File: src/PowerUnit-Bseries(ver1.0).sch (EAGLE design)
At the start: 46 parts

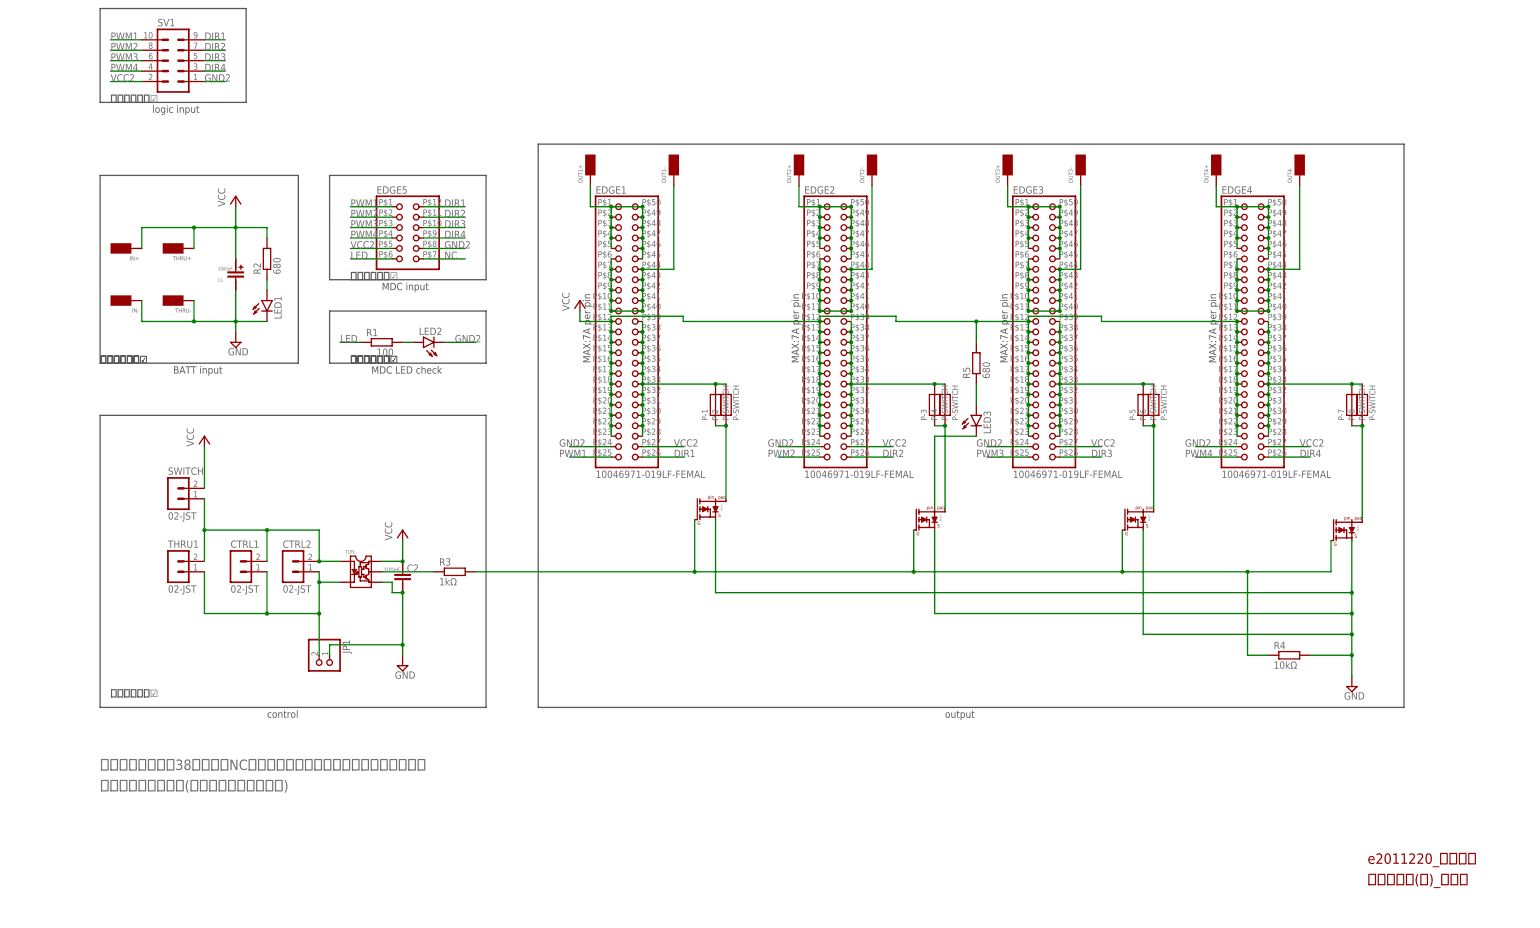
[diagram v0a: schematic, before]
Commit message: 再設計 Edgeコネクタを40Pにした
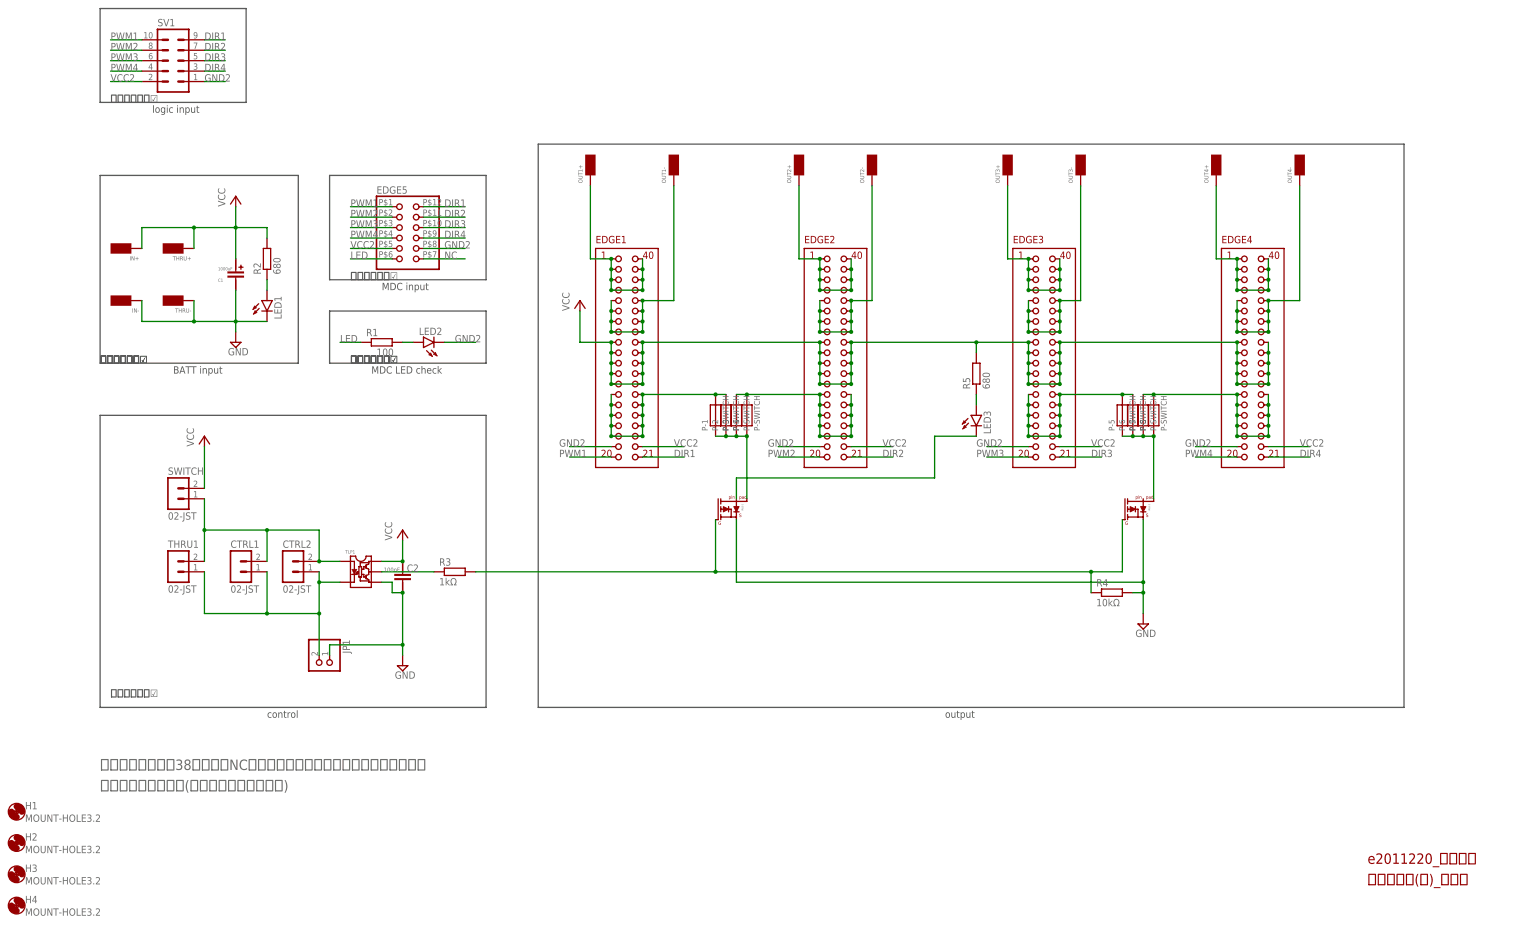
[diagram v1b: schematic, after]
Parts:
- removed IRLB-3, IRLB-4: IRLB3813_2, OKUDA_libraries:IRLB3813_2
- added H1, H2, H3, H4: MOUNT-HOLE3.2, holes:MOUNT-HOLE3.2
- EDGE1, EDGE2, EDGE3, EDGE4: value 10046971-019LF-FEMAL -> EDGE20X2; device 10046971-019LF-FEMAL:10046971-019LF-FEMAL -> Edge20x2:EDGE20X2
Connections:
- removed net N$10: EDGE4.P1, EDGE4.P2, EDGE4.P3, EDGE4.P4, EDGE4.P45, EDGE4.P46, EDGE4.P47, EDGE4.P48, EDGE4.P49, EDGE4.P5, EDGE4.P50, OUT4+.P$1
- removed net N$12: IRLB-4.PD, P-7.P$2, P-8.P$2
- removed net N$13: EDGE4.P10, EDGE4.P11, EDGE4.P40, EDGE4.P41, EDGE4.P42, EDGE4.P43, EDGE4.P44, EDGE4.P6, EDGE4.P7, EDGE4.P8, EDGE4.P9, OUT4-.P$1
- removed net N$14: EDGE3.P28, EDGE3.P29, EDGE3.P30, EDGE3.P31, EDGE3.P32, EDGE3.P33, EDGE3.P34, EDGE3.P35, EDGE3.P36, EDGE3.P37, EDGE3.P38, EDGE3.P39, P-5.P$1, P-6.P$1
- removed net N$15: IRLB-3.PD, P-5.P$2, P-6.P$2
- removed net N$25: EDGE1.P28, EDGE1.P29, EDGE1.P30, EDGE1.P31, EDGE1.P32, EDGE1.P33, EDGE1.P34, EDGE1.P35, EDGE1.P36, EDGE1.P37, EDGE1.P38, EDGE1.P39, P-1.P$1, P-2.P$1
- removed net N$26: EDGE2.P28, EDGE2.P29, EDGE2.P30, EDGE2.P31, EDGE2.P32, EDGE2.P33, EDGE2.P34, EDGE2.P35, EDGE2.P36, EDGE2.P37, EDGE2.P38, EDGE2.P39, P-3.P$1, P-4.P$1
- new net N$23: IRLB-1.PD, P-1.P$2, P-2.P$2, P-3.P$2, P-4.P$2
- new net N$27: IRLB-2.PD, P-5.P$2, P-6.P$2, P-7.P$2, P-8.P$2
- new net N$28: EDGE1.P$1, EDGE1.P$2, EDGE1.P$3, EDGE1.P$37, EDGE1.P$38, EDGE1.P$39, EDGE1.P$4, EDGE1.P$40, OUT1+.P$1
- new net N$34: EDGE2.P$14, EDGE2.P$15, EDGE2.P$16, EDGE2.P$17, EDGE2.P$18, EDGE2.P$23, EDGE2.P$24, EDGE2.P$25, EDGE2.P$26, EDGE2.P$27, P-3.P$1, P-4.P$1
- new net N$35: EDGE3.P$1, EDGE3.P$2, EDGE3.P$3, EDGE3.P$37, EDGE3.P$38, EDGE3.P$39, EDGE3.P$4, EDGE3.P$40, OUT3+.P$1
- net DIR1: now also EDGE1.P$21; no longer EDGE1.P26
- net DIR2: now also EDGE2.P$21; no longer EDGE2.P26
- net DIR3: now also EDGE3.P$21; no longer EDGE3.P26
- net DIR4: now also EDGE4.P$21; no longer EDGE4.P26
- net GND: no longer IRLB-3.S, IRLB-4.S
- net GND2: now also EDGE1.P$19, EDGE2.P$19, EDGE3.P$19, EDGE4.P$19; no longer EDGE1.P24, EDGE2.P24, EDGE3.P24, EDGE4.P24
- net N$1: now also EDGE1.P$33, EDGE1.P$34, EDGE1.P$35, EDGE1.P$36, EDGE1.P$5, EDGE1.P$6, EDGE1.P$7, EDGE1.P$8; no longer EDGE1.P10, EDGE1.P11, EDGE1.P40, EDGE1.P41, EDGE1.P42, EDGE1.P43, EDGE1.P44, EDGE1.P6, EDGE1.P7, EDGE1.P8, EDGE1.P9
- net N$11: now also EDGE4.P$14, EDGE4.P$15, EDGE4.P$16, EDGE4.P$17, EDGE4.P$18, EDGE4.P$23, EDGE4.P$24, EDGE4.P$25, EDGE4.P$26, EDGE4.P$27, P-7.P$1, P-8.P$1; no longer IRLB-2.PD, P-3.P$2, P-4.P$2
- net N$2: now also EDGE2.P$33, EDGE2.P$34, EDGE2.P$35, EDGE2.P$36, EDGE2.P$5, EDGE2.P$6, EDGE2.P$7, EDGE2.P$8; no longer EDGE2.P10, EDGE2.P11, EDGE2.P40, EDGE2.P41, EDGE2.P42, EDGE2.P43, EDGE2.P44, EDGE2.P6, EDGE2.P7, EDGE2.P8, EDGE2.P9
- net N$22: no longer IRLB-3.G, IRLB-4.G
- net N$24: now also IRLB-1.D; no longer IRLB-2.D
- net N$4: now also EDGE1.P$14, EDGE1.P$15, EDGE1.P$16, EDGE1.P$17, EDGE1.P$18, EDGE1.P$23, EDGE1.P$24, EDGE1.P$25, EDGE1.P$26, EDGE1.P$27, P-1.P$1, P-2.P$1; no longer EDGE1.P1, EDGE1.P2, EDGE1.P3, EDGE1.P4, EDGE1.P45, EDGE1.P46, EDGE1.P47, EDGE1.P48, EDGE1.P49, EDGE1.P5, EDGE1.P50, OUT1+.P$1
- net N$5: now also EDGE2.P$1, EDGE2.P$2, EDGE2.P$3, EDGE2.P$37, EDGE2.P$38, EDGE2.P$39, EDGE2.P$4, EDGE2.P$40; no longer EDGE2.P1, EDGE2.P2, EDGE2.P3, EDGE2.P4, EDGE2.P45, EDGE2.P46, EDGE2.P47, EDGE2.P48, EDGE2.P49, EDGE2.P5, EDGE2.P50
- net N$6: now also EDGE4.P$33, EDGE4.P$34, EDGE4.P$35, EDGE4.P$36, EDGE4.P$5, EDGE4.P$6, EDGE4.P$7, EDGE4.P$8, OUT4-.P$1; no longer EDGE3.P1, EDGE3.P2, EDGE3.P3, EDGE3.P4, EDGE3.P45, EDGE3.P46, EDGE3.P47, EDGE3.P48, EDGE3.P49, EDGE3.P5, EDGE3.P50, OUT3+.P$1
- net N$7: now also EDGE3.P$33, EDGE3.P$34, EDGE3.P$35, EDGE3.P$36, EDGE3.P$5, EDGE3.P$6, EDGE3.P$7, EDGE3.P$8, OUT3-.P$1; no longer IRLB-1.PD, P-1.P$2, P-2.P$2
- net N$8: now also EDGE4.P$1, EDGE4.P$2, EDGE4.P$3, EDGE4.P$37, EDGE4.P$38, EDGE4.P$39, EDGE4.P$4, EDGE4.P$40, OUT4+.P$1; no longer EDGE4.P28, EDGE4.P29, EDGE4.P30, EDGE4.P31, EDGE4.P32, EDGE4.P33, EDGE4.P34, EDGE4.P35, EDGE4.P36, EDGE4.P37, EDGE4.P38, EDGE4.P39, P-7.P$1, P-8.P$1
- net N$9: now also EDGE3.P$14, EDGE3.P$15, EDGE3.P$16, EDGE3.P$17, EDGE3.P$18, EDGE3.P$23, EDGE3.P$24, EDGE3.P$25, EDGE3.P$26, EDGE3.P$27, P-5.P$1, P-6.P$1; no longer EDGE3.P10, EDGE3.P11, EDGE3.P40, EDGE3.P41, EDGE3.P42, EDGE3.P43, EDGE3.P44, EDGE3.P6, EDGE3.P7, EDGE3.P8, EDGE3.P9, OUT3-.P$1
- net PWM1: now also EDGE1.P$20; no longer EDGE1.P25
- net PWM2: now also EDGE2.P$20; no longer EDGE2.P25
- net PWM3: now also EDGE3.P$20; no longer EDGE3.P25
- net PWM4: now also EDGE4.P$20; no longer EDGE4.P25
- net VCC: now also EDGE1.P$10, EDGE1.P$11, EDGE1.P$12, EDGE1.P$13, EDGE1.P$28, EDGE1.P$29, EDGE1.P$30, EDGE1.P$31, EDGE1.P$32, EDGE1.P$9, EDGE2.P$10, EDGE2.P$11, EDGE2.P$12, EDGE2.P$13, EDGE2.P$28, EDGE2.P$29, EDGE2.P$30, EDGE2.P$31, EDGE2.P$32, EDGE2.P$9, EDGE3.P$10, EDGE3.P$11, EDGE3.P$12, EDGE3.P$13, EDGE3.P$28, EDGE3.P$29, EDGE3.P$30, EDGE3.P$31, EDGE3.P$32, EDGE3.P$9, EDGE4.P$10, EDGE4.P$11, EDGE4.P$12, EDGE4.P$13, EDGE4.P$28, EDGE4.P$29, EDGE4.P$30, EDGE4.P$31, EDGE4.P$32, EDGE4.P$9; no longer EDGE1.P12, EDGE1.P13, EDGE1.P14, EDGE1.P15, EDGE1.P16, EDGE1.P17, EDGE1.P18, EDGE1.P19, EDGE1.P20, EDGE1.P21, EDGE1.P22, EDGE1.P23, EDGE2.P12, EDGE2.P13, EDGE2.P14, EDGE2.P15, EDGE2.P16, EDGE2.P17, EDGE2.P18, EDGE2.P19, EDGE2.P20, EDGE2.P21, EDGE2.P22, EDGE2.P23, EDGE3.P12, EDGE3.P13, EDGE3.P14, EDGE3.P15, EDGE3.P16, EDGE3.P17, EDGE3.P18, EDGE3.P19, EDGE3.P20, EDGE3.P21, EDGE3.P22, EDGE3.P23, EDGE4.P12, EDGE4.P13, EDGE4.P14, EDGE4.P15, EDGE4.P16, EDGE4.P17, EDGE4.P18, EDGE4.P19, EDGE4.P20, EDGE4.P21, EDGE4.P22, EDGE4.P23
- net VCC2: now also EDGE1.P$22, EDGE2.P$22, EDGE3.P$22, EDGE4.P$22; no longer EDGE1.P27, EDGE2.P27, EDGE3.P27, EDGE4.P27
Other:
- moved on the sheet: IRLB-1, IRLB-2, P-1, P-2, P-3, P-4, P-5, P-6, P-7, P-8, R4, R5
